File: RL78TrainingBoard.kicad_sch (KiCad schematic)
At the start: 85 parts, among them J1 USB_B_Mini, J2 DSub9pin_Male, J3 Debugger, J4 OLED, Q1 AO3400A, Q2 NJL7502L, SW1 SW_A, SW2 SW_B, SW3 SW_C, SW4 SW_D, SW5 RESET_SW, SW6 USER_SW, U1 TBD62783A, U2 FT230XS, U3 ADM3202, U4 SC1602B, U5 RL78G13_64pin, U6 LM60, U7 YMZ294, U8 HT82V739, Y1 32.768kHz

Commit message: フットプリント作成
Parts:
- added C17: 100uF, RL78TrainingBoard:3216Metric, symbol Device:C_Small
- added C2, C3: 39pF, RL78TrainingBoard:1608Metric, symbol Device:C_Small
- C1, D1, D10, D2, D3, D4, D5, D6, D7, D8, D9, L1, R1, R13, R14, R15, R16, R17, R18, R19, R2, R20, R21, R22, R23, R24, R25, R3, R4, R5, R6, R7, R8, R9: footprint (none) -> RL78TrainingBoard:1608Metric
- C10: renamed from C8; footprint (none) -> RL78TrainingBoard:1608Metric
- C11: renamed from C9; footprint (none) -> RL78TrainingBoard:1608Metric
- C12: renamed from C7; footprint (none) -> RL78TrainingBoard:1005Metric
- C13: renamed from C10; footprint (none) -> RL78TrainingBoard:1608Metric
- C14: renamed from C11; footprint (none) -> RL78TrainingBoard:1608Metric
- C15: renamed from C12; footprint (none) -> RL78TrainingBoard:1608Metric
- C16: renamed from C13; footprint (none) -> RL78TrainingBoard:1608Metric
- C18: renamed from C14; footprint (none) -> RL78TrainingBoard:1608Metric
- C19: renamed from C15; footprint (none) -> RL78TrainingBoard:1608Metric
- C20: renamed from C16; footprint (none) -> RL78TrainingBoard:1608Metric
- C21: renamed from C17; footprint (none) -> RL78TrainingBoard:1608Metric
- C4: renamed from C18; value 47uF -> 100uF; footprint (none) -> RL78TrainingBoard:CP_Elec_6.3x7.7
- C5: renamed from C2; footprint (none) -> RL78TrainingBoard:1608Metric
- C6: renamed from C3; footprint (none) -> RL78TrainingBoard:1608Metric
- C7: renamed from C4; footprint (none) -> RL78TrainingBoard:1608Metric
- C8: renamed from C5; footprint (none) -> RL78TrainingBoard:1608Metric
- C9: renamed from C6; footprint (none) -> RL78TrainingBoard:1005Metric
- F1: footprint (none) -> RL78TrainingBoard:3216Metric
- J1: footprint (none) -> RL78TrainingBoard:UX60SC-MB-5ST
- J2: footprint (none) -> RL78TrainingBoard:DSUB-9_Male_Horizontal_P2.77x2.84mm_EdgePinOffset7.70mm_Housed_MountingHolesOffset9.12mm
- J3: footprint (none) -> RL78TrainingBoard:IDC-Header_2x07_P2.54mm_Vertical
- J4: footprint (none) -> RL78TrainingBoard:OLED
- JP1, JP2: footprint (none) -> RL78TrainingBoard:Jumper_1x03_P2.54mm
- LS1: footprint (none) -> RL78TrainingBoard:PKMCS0909E4000-R1
- LS2: footprint (none) -> RL78TrainingBoard:UM1515IA085008
- Q1: footprint (none) -> RL78TrainingBoard:SOT-23
- Q2: footprint (none) -> RL78TrainingBoard:NJL7502L
- R10: renamed from R12; footprint (none) -> RL78TrainingBoard:1608Metric
- R11: renamed from R10; footprint (none) -> RL78TrainingBoard:1608Metric
- R12: renamed from R11; footprint (none) -> RL78TrainingBoard:1608Metric
- RV1, RV2: footprint (none) -> RL78TrainingBoard:RV
- RV3: value LCD_Contrast -> 10k; footprint (none) -> RL78TrainingBoard:TSR-3323S
- RV4: footprint (none) -> RL78TrainingBoard:TSR-3386K
- RV5: footprint (none) -> RL78TrainingBoard:Volume_RK10J
- SW1, SW2, SW3, SW4, SW6: footprint (none) -> RL78TrainingBoard:SW_PUSH_6mm
- SW5: footprint (none) -> RL78TrainingBoard:SW_TVAF06
- U1: footprint (none) -> RL78TrainingBoard:SOP-18_7x12.5mm_P1.27mm
- U2: footprint (none) -> RL78TrainingBoard:SSOP-16_3.9x4.9mm_P0.635mm
- U3: footprint (none) -> RL78TrainingBoard:TSSOP-16-1EP_4.4x5mm_P0.65mm
- U4: footprint (none) -> RL78TrainingBoard:SC1602
- U5: footprint (none) -> RL78TrainingBoard:LQFP-64-12x12mm-P0.65mm_FusionPCB
- U6: footprint Package_TO_SOT_SMD:SOT-23 -> RL78TrainingBoard:SOT-23
- U7: footprint (none) -> RL78TrainingBoard:DIP-18_W7.62mm_Socket
- U8: footprint (none) -> RL78TrainingBoard:SOP-8_3.9x4.9mm_P1.27mm
- Y1: footprint (none) -> RL78TrainingBoard:Crystal_SMD_3215-2Pin
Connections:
- net +5V: now also C17.1
- net DM: now also C3.1
- net DP: now also C2.1
- net GND: now also C17.2, C2.2, C3.2
- net Light renamed LIGHT
- net Temp renamed TEMP
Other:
- moved on the sheet: C1, C4, C5, D1, D2, D3, D4, D5, D6, D7, D8, JP1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

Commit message: 基板設計(部品仮配置)
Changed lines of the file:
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@@
     )
   )
-  (global_label "YMZ294_WR" (shape input) (at 242.57 88.9 270) (fields_autoplaced)
+  (global_label "YMZ294_WR" (shape input) (at 242.57 88.9 180) (fields_autoplaced)
     (effects (font (size 1.27 1.27)) (justify right))
-    (property "シート間のリファレンス" "${INTERSHEET_REFS}" (id 0) (at 242.4906 102.3802 90)
+    (property "シート間のリファレンス" "${INTERSHEET_REFS}" (id 0) (at 229.0898 88.8206 0)
       (effects (font (size 1.27 1.27)) (justify right) hide)
     )

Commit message: 部品見直し
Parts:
- removed JP1: UART_TXD_Jumper, RL78TrainingBoard:Jumper_1x03_P2.54mm, symbol Jumper:Jumper_3_Bridged12
- removed JP2: UART_RXD_Jumper, RL78TrainingBoard:Jumper_1x03_P2.54mm, symbol Jumper:Jumper_3_Bridged12
- added SW7: SW_SPDT, RL78TrainingBoard:2MS1-T2-B4-M2-Q-E-S, symbol Switch:SW_SPDT
- added SW8: SW_DPDT_x2, RL78TrainingBoard:IS-2235-G, symbol Switch:SW_DPDT_x2
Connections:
- net +5V: now also L1.2; no longer J3.8 (VDD), J3.9 (EMVDD), L1.1
- net RS232C_RXD: now also SW8.6 (C)
- net RS232C_TXD: now also SW8.3 (C)
- net UART_RXD: now also SW8.5 (B)
- net UART_TXD: now also SW8.2 (B)
- net USB_RXD: now also SW8.4 (A)
- net USB_TXD: now also SW8.1 (A)
- net at F1.2: now also L1.1; no longer J1.1 (VBUS)
- net at F1.1: now also SW7.1 (A); no longer L1.2
- new net VBUS: J1.1 (VBUS), J3.8 (VDD), J3.9 (EMVDD), SW7.2 (B)
- no-connect marks 30 -> 31
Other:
- moved on the sheet: C4, F1, L1

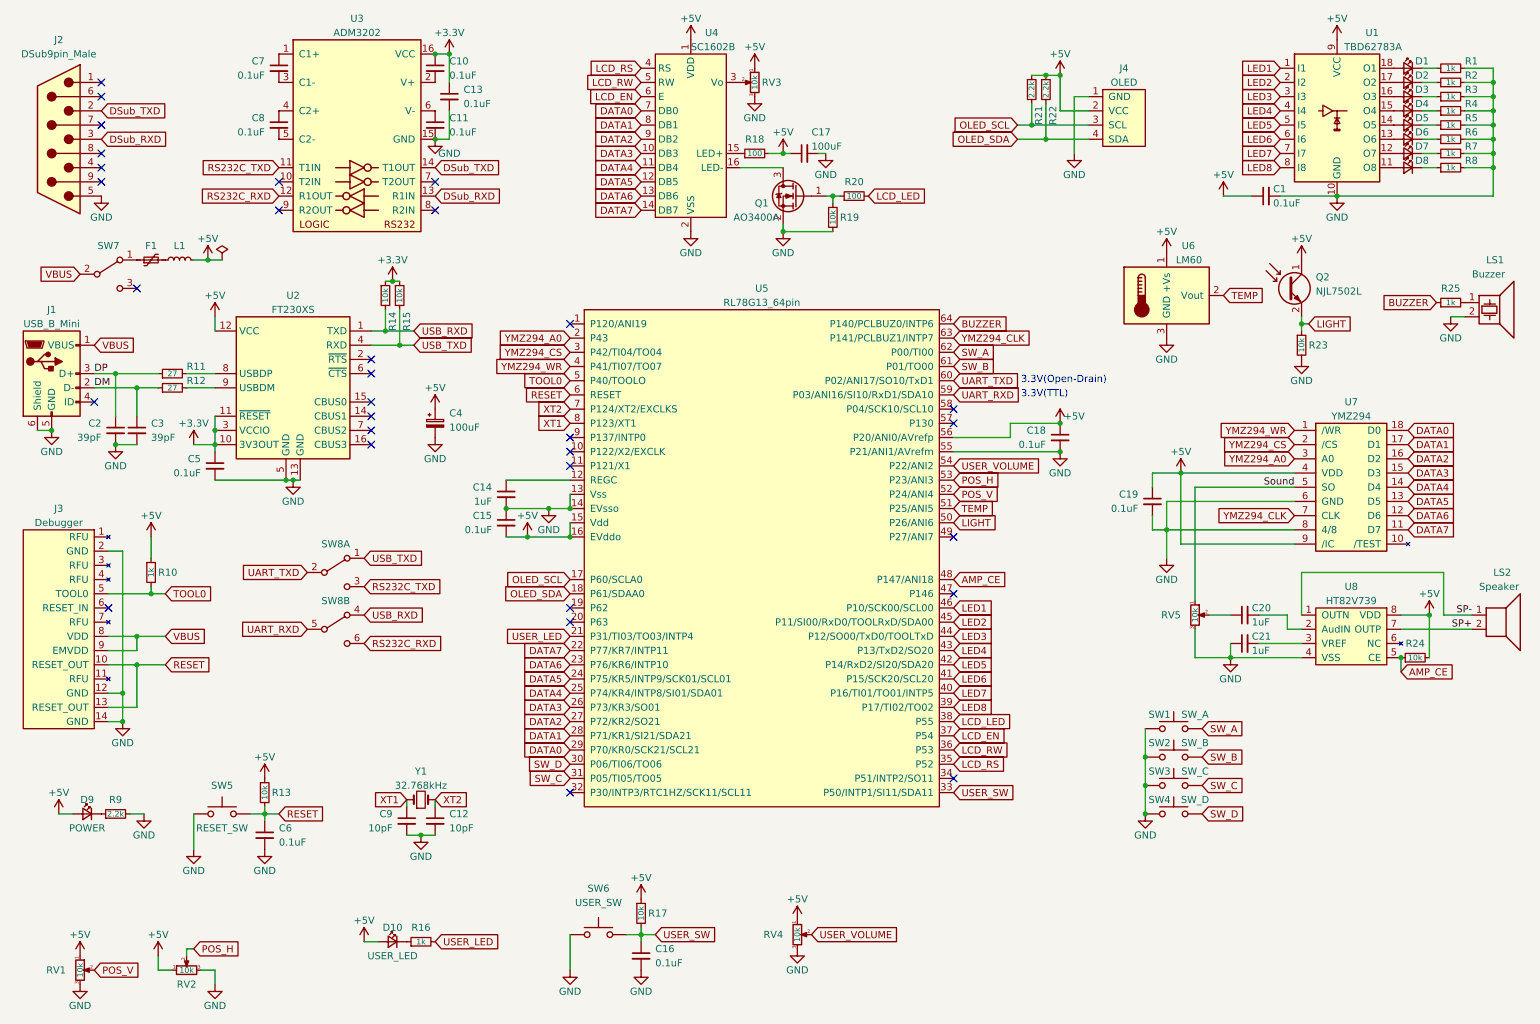
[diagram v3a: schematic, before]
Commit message: 配線作成
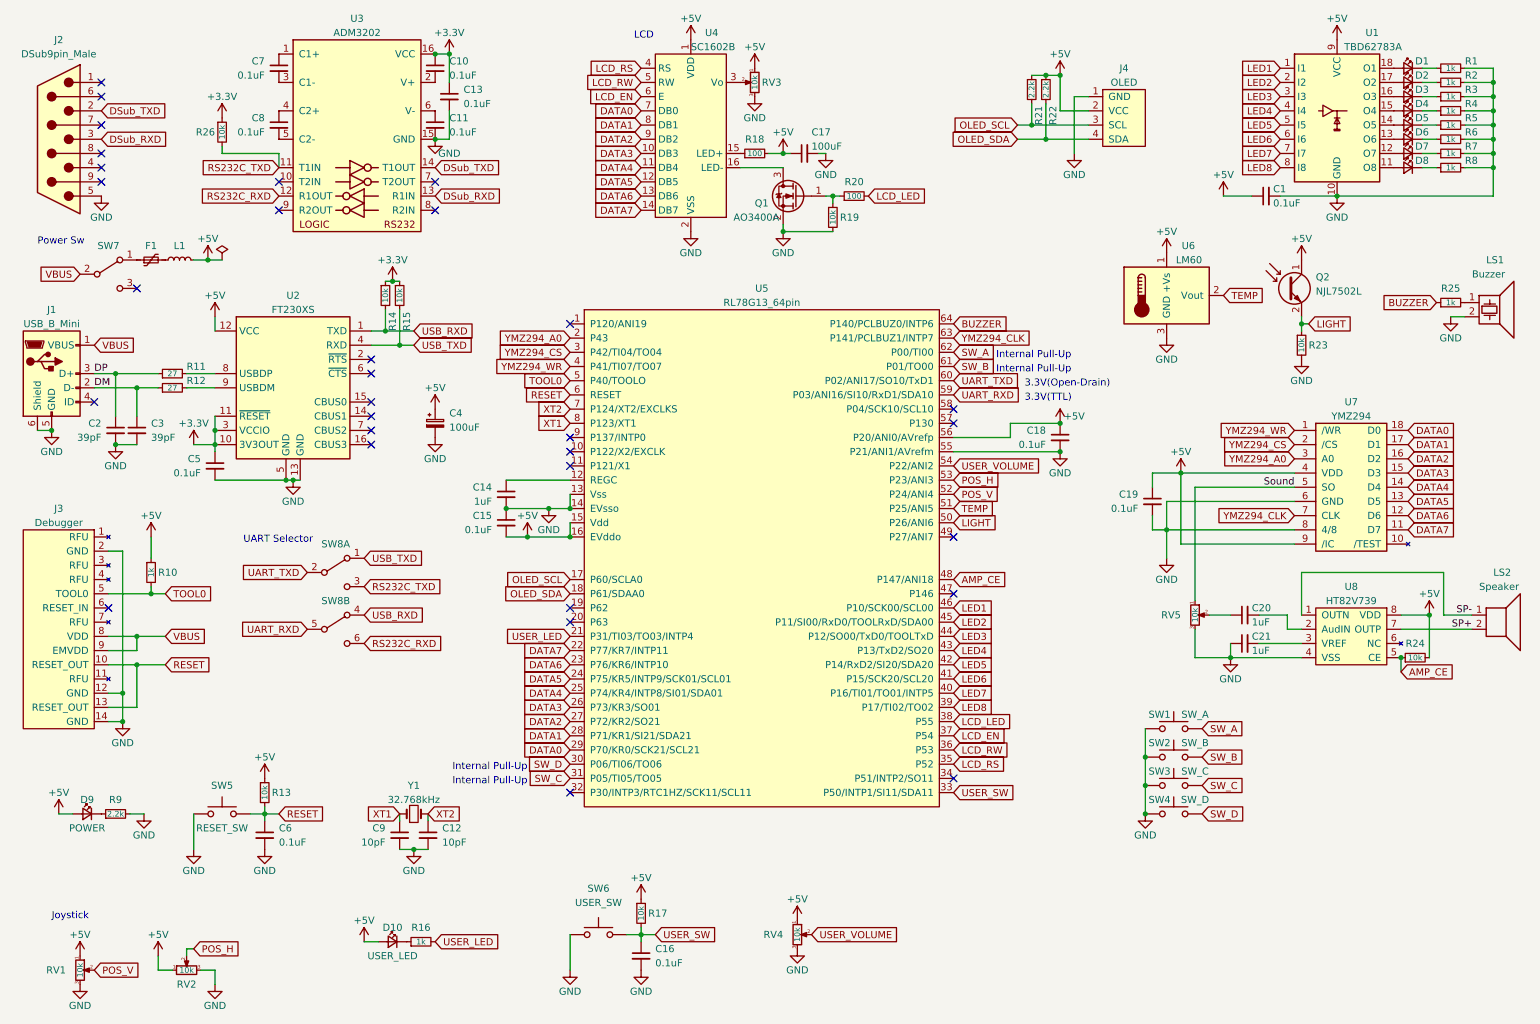
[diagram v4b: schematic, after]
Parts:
- added R26: 10k, RL78TrainingBoard:1608Metric, symbol Device:R_Small
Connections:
- net +3V3: now also R26.1
- net RS232C_TXD: now also R26.2
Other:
- note added: "Internal Pull-Up"
- note added: "Joystick"
- note added: "LCD"
- note added: "Power Sw"
- note added: "UART Selector"
- moved on the sheet: C12, C9, Y1
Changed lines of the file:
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@@
   (junction (at 88.9 21.59) (diameter 0) (color 0 0 0 0)
   )
-  (junction (at 86.36 161.29) (diameter 0) (color 0 0 0 0)
+  (junction (at 85.09 163.83) (diameter 0) (color 0 0 0 0)
   )
   (junction (at 20.32 88.9) (diameter 0) (color 0 0 0 0)
@@
     (stroke (width 0) (type default) (color 0 0 0 0))
   )
-  (wire (pts (xy 83.82 154.94) (xy 83.82 156.21))
+  (wire (pts (xy 82.55 157.48) (xy 82.55 158.75))
     (stroke (width 0) (type default) (color 0 0 0 0))
   )
@@
     (stroke (width 0) (type default) (color 0 0 0 0))
   )
+  (wire (pts (xy 50.8 38.1) (xy 50.8 39.37))
+    (stroke (width 0) (type default) (color 0 0 0 0))
+  )
   (wire (pts (xy 217.17 106.68) (xy 219.71 106.68))
     (stroke (width 0) (type default) (color 0 0 0 0))
@@
     (stroke (width 0) (type default) (color 0 0 0 0))
   )
+  (wire (pts (xy 50.8 39.37) (xy 60.96 39.37))
+    (stroke (width 0) (type default) (color 0 0 0 0))
+  )
   (wire (pts (xy 45.72 91.44) (xy 49.53 91.44))
     (stroke (width 0) (type default) (color 0 0 0 0))
@@
     (stroke (width 0) (type default) (color 0 0 0 0))
   )
-  (wire (pts (xy 83.82 161.29) (xy 86.36 161.29))
+  (wire (pts (xy 82.55 163.83) (xy 85.09 163.83))
     (stroke (width 0) (type default) (color 0 0 0 0))
   )
@@
     (stroke (width 0) (type default) (color 0 0 0 0))
   )
+  (wire (pts (xy 60.96 39.37) (xy 60.96 41.91))
+    (stroke (width 0) (type default) (color 0 0 0 0))
+  )
   (wire (pts (xy 77.47 73.66) (xy 82.55 73.66))
     (stroke (width 0) (type default) (color 0 0 0 0))
@@
     (stroke (width 0) (type default) (color 0 0 0 0))
   )
-  (wire (pts (xy 88.9 154.94) (xy 88.9 156.21))
+  (wire (pts (xy 87.63 157.48) (xy 87.63 158.75))
     (stroke (width 0) (type default) (color 0 0 0 0))
   )
-  (wire (pts (xy 86.36 161.29) (xy 88.9 161.29))
+  (wire (pts (xy 85.09 163.83) (xy 87.63 163.83))
     (stroke (width 0) (type default) (color 0 0 0 0))
   )
@@
     (stroke (width 0) (type default) (color 0 0 0 0))
   )
-  (text "3.3V(Open-Drain)" (at 193.675 80.645 0)
+  (text "3.3V(Open-Drain)" (at 194.31 81.28 0)
+    (effects (font (size 1.27 1.27)) (justify left bottom))
+  )
+  (text "LCD" (at 124.46 19.05 0)
+    (effects (font (size 1.27 1.27)) (justify left bottom))
+  )
+  (text "3.3V(TTL)" (at 194.31 83.82 0)
+    (effects (font (size 1.27 1.27)) (justify left bottom))
+  )
+  (text "Internal Pull-Up" (at 189.23 76.2 0)
     (effects (font (size 1.27 1.27)) (justify left bottom))
   )
-  (text "3.3V(TTL)" (at 193.675 83.185 0)
+  (text "Internal Pull-Up" (at 189.23 78.74 0)
+    (effects (font (size 1.27 1.27)) (justify left bottom))
+  )
+  (text "Internal Pull-Up" (at 105.41 152.4 180)
+    (effects (font (size 1.27 1.27)) (justify right bottom))
+  )
+  (text "Joystick" (at 20.32 176.53 0)
+    (effects (font (size 1.27 1.27)) (justify left bottom))
+  )
+  (text "Internal Pull-Up" (at 105.41 149.86 180)
+    (effects (font (size 1.27 1.27)) (justify right bottom))
+  )
+  (text "UART Selector" (at 54.61 109.22 0)
+    (effects (font (size 1.27 1.27)) (justify left bottom))
+  )
+  (text "Power Sw" (at 17.78 55.88 0)
     (effects (font (size 1.27 1.27)) (justify left bottom))
   )
@@
     )
   )
-  (global_label "XT2" (shape input) (at 88.9 154.94 0) (fields_autoplaced)
+  (global_label "XT2" (shape input) (at 87.63 157.48 0) (fields_autoplaced)
     (effects (font (size 1.27 1.27)) (justify left))
-    (property "シート間のリファレンス" "${INTERSHEET_REFS}" (id 0) (at 94.6998 154.8606 0)
+    (property "シート間のリファレンス" "${INTERSHEET_REFS}" (id 0) (at 93.4298 157.4006 0)
       (effects (font (size 1.27 1.27)) (justify left) hide)
     )
@@
     )
   )
-  (global_label "XT1" (shape input) (at 83.82 154.94 180) (fields_autoplaced)
+  (global_label "XT1" (shape input) (at 82.55 157.48 180) (fields_autoplaced)
     (effects (font (size 1.27 1.27)) (justify right))
-    (property "シート間のリファレンス" "${INTERSHEET_REFS}" (id 0) (at 78.0202 154.8606 0)
+    (property "シート間のリファレンス" "${INTERSHEET_REFS}" (id 0) (at 76.7502 157.4006 0)
       (effects (font (size 1.27 1.27)) (justify right) hide)
     )
@@
     (pin "1")
   )
-  (symbol (lib_id "Device:Crystal_Small") (at 86.36 154.94 0) (unit 1)
+  (symbol (lib_id "Device:Crystal_Small") (at 85.09 157.48 0) (unit 1)
     (in_bom yes) (on_board yes)
-    (property "Reference" "Y1" (id 0) (at 86.36 149.86 0))
-    (property "Value" "32.768kHz" (id 1) (at 86.36 152.4 0))
-    (property "Footprint" "RL78TrainingBoard:Crystal_SMD_3215-2Pin" (id 2) (at 86.36 154.94 0)
+    (property "Reference" "Y1" (id 0) (at 85.09 152.4 0))
+    (property "Value" "32.768kHz" (id 1) (at 85.09 154.94 0))
+    (property "Footprint" "RL78TrainingBoard:Crystal_SMD_3215-2Pin" (id 2) (at 85.09 157.48 0)
       (effects (font (size 1.27 1.27)) hide)
     )
-    (property "Datasheet" "~" (id 3) (at 86.36 154.94 0)
+    (property "Datasheet" "~" (id 3) (at 85.09 157.48 0)
       (effects (font (size 1.27 1.27)) hide)
     )
@@
     (pin "9")
   )
-  (symbol (lib_id "Device:C_Small") (at 88.9 158.75 0) (unit 1)
+  (symbol (lib_id "Device:C_Small") (at 87.63 161.29 0) (unit 1)
     (in_bom yes) (on_board yes) (fields_autoplaced)
-    (property "Reference" "C12" (id 0) (at 91.44 157.4862 0)
+    (property "Reference" "C12" (id 0) (at 90.17 160.0262 0)
       (effects (font (size 1.27 1.27)) (justify left))
     )
-    (property "Value" "10pF" (id 1) (at 91.44 160.0262 0)
+    (property "Value" "10pF" (id 1) (at 90.17 162.5662 0)
       (effects (font (size 1.27 1.27)) (justify left))
     )
-    (property "Footprint" "RL78TrainingBoard:1005Metric" (id 2) (at 88.9 158.75 0)
+    (property "Footprint" "RL78TrainingBoard:1005Metric" (id 2) (at 87.63 161.29 0)
       (effects (font (size 1.27 1.27)) hide)
     )
-    (property "Datasheet" "~" (id 3) (at 88.9 158.75 0)
+    (property "Datasheet" "~" (id 3) (at 87.63 161.29 0)
       (effects (font (size 1.27 1.27)) hide)
     )
@@
     (pin "3")
   )
+  (symbol (lib_id "power:+3.3V") (at 50.8 33.02 0) (unit 1)
+    (in_bom yes) (on_board yes)
+    (property "Reference" "#PWR057" (id 0) (at 50.8 36.83 0)
+      (effects (font (size 1.27 1.27)) hide)
+    )
+    (property "Value" "+3.3V" (id 1) (at 50.8 29.21 0))
+    (property "Footprint" "" (id 2) (at 50.8 33.02 0)
+      (effects (font (size 1.27 1.27)) hide)
+    )
+    (property "Datasheet" "" (id 3) (at 50.8 33.02 0)
+      (effects (font (size 1.27 1.27)) hide)
+    )
+    (pin "1")
+  )
   (symbol (lib_id "power:PWR_FLAG") (at 50.8 58.42 0) (unit 1)
     (in_bom yes) (on_board yes) (fields_autoplaced)
@@
     (pin "1")
   )
+  (symbol (lib_id "Device:R_Small") (at 50.8 35.56 0) (unit 1)
+    (in_bom yes) (on_board yes)
+    (property "Reference" "R26" (id 0) (at 49.53 35.56 0)
+      (effects (font (size 1.27 1.27)) (justify right))
+    )
+    (property "Value" "10k" (id 1) (at 50.8 35.56 90)
+      (effects (font (size 1.016 1.016)))
+    )
+    (property "Footprint" "RL78TrainingBoard:1608Metric" (id 2) (at 50.8 35.56 0)
+      (effects (font (size 1.27 1.27)) hide)
+    )
+    (property "Datasheet" "~" (id 3) (at 50.8 35.56 0)
+      (effects (font (size 1.27 1.27)) hide)
+    )
+    (pin "1")
+    (pin "2")
+  )
   (symbol (lib_id "power:+3.3V") (at 45.72 91.44 0) (unit 1)
     (in_bom yes) (on_board yes)
@@
     (pin "1")
   )
-  (symbol (lib_id "Device:C_Small") (at 83.82 158.75 0) (mirror y) (unit 1)
+  (symbol (lib_id "Device:C_Small") (at 82.55 161.29 0) (mirror y) (unit 1)
     (in_bom yes) (on_board yes)
-    (property "Reference" "C9" (id 0) (at 81.28 157.48 0)
+    (property "Reference" "C9" (id 0) (at 80.01 160.02 0)
       (effects (font (size 1.27 1.27)) (justify left))
     )
-    (property "Value" "10pF" (id 1) (at 81.28 160.02 0)
+    (property "Value" "10pF" (id 1) (at 80.01 162.56 0)
       (effects (font (size 1.27 1.27)) (justify left))
     )
-    (property "Footprint" "RL78TrainingBoard:1005Metric" (id 2) (at 83.82 158.75 0)
+    (property "Footprint" "RL78TrainingBoard:1005Metric" (id 2) (at 82.55 161.29 0)
       (effects (font (size 1.27 1.27)) hide)
     )
-    (property "Datasheet" "~" (id 3) (at 83.82 158.75 0)
+    (property "Datasheet" "~" (id 3) (at 82.55 161.29 0)
       (effects (font (size 1.27 1.27)) hide)
     )
@@
     (pin "2")
   )
-  (symbol (lib_id "power:GND") (at 86.36 161.29 0) (unit 1)
+  (symbol (lib_id "power:GND") (at 85.09 163.83 0) (unit 1)
     (in_bom yes) (on_board yes)
-    (property "Reference" "#PWR027" (id 0) (at 86.36 167.64 0)
+    (property "Reference" "#PWR027" (id 0) (at 85.09 170.18 0)
       (effects (font (size 1.27 1.27)) hide)
     )
-    (property "Value" "GND" (id 1) (at 86.36 165.1 0))
-    (property "Footprint" "" (id 2) (at 86.36 161.29 0)
+    (property "Value" "GND" (id 1) (at 85.09 167.64 0))
+    (property "Footprint" "" (id 2) (at 85.09 163.83 0)
       (effects (font (size 1.27 1.27)) hide)
     )
-    (property "Datasheet" "" (id 3) (at 86.36 161.29 0)
+    (property "Datasheet" "" (id 3) (at 85.09 163.83 0)
       (effects (font (size 1.27 1.27)) hide)
     )
@@
       (reference "#PWR056") (unit 1) (value "GND") (footprint "")
     )
+    (path "/1c8092d0-448a-48c6-a311-6c6c310eb312"
+      (reference "#PWR057") (unit 1) (value "+3.3V") (footprint "")
+    )
     (path "/fe65c247-9c95-494a-ad4f-90b729c51f04"
       (reference "C1") (unit 1) (value "0.1uF") (footprint "RL78TrainingBoard:1608Metric")
@@
       (reference "R25") (unit 1) (value "1k") (footprint "RL78TrainingBoard:1608Metric")
     )
+    (path "/56e37f25-2d9b-4d4f-bf1b-84bbb1161f3a"
+      (reference "R26") (unit 1) (value "10k") (footprint "RL78TrainingBoard:1608Metric")
+    )
     (path "/344d6075-c2a7-490e-8fe1-7804e771e777"
